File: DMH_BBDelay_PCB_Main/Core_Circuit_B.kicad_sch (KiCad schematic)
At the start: 73 parts, among them Q8 J113, SW1 SW_DPDT_3way_x2, SW2 SW_DPDT_x2, SW4 SW_SPDT, U18 CD4053B, U5 TL074, U6 TL074, U7 V3205, U8 CD4046, U9 40106

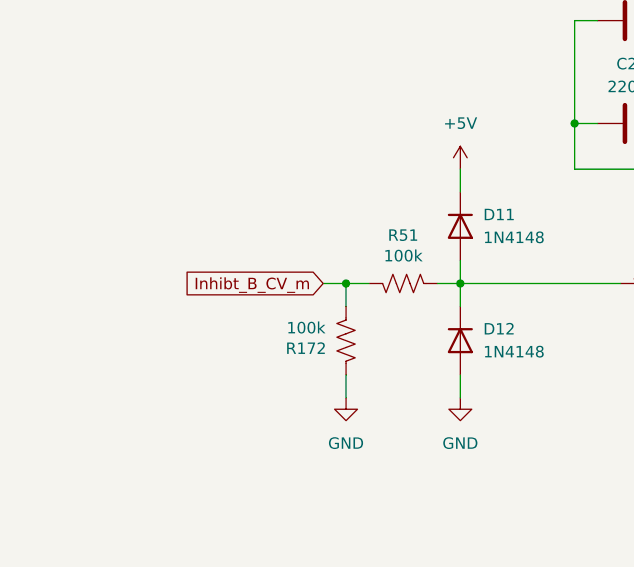
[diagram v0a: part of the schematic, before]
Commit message: Added J200 connections in IO page
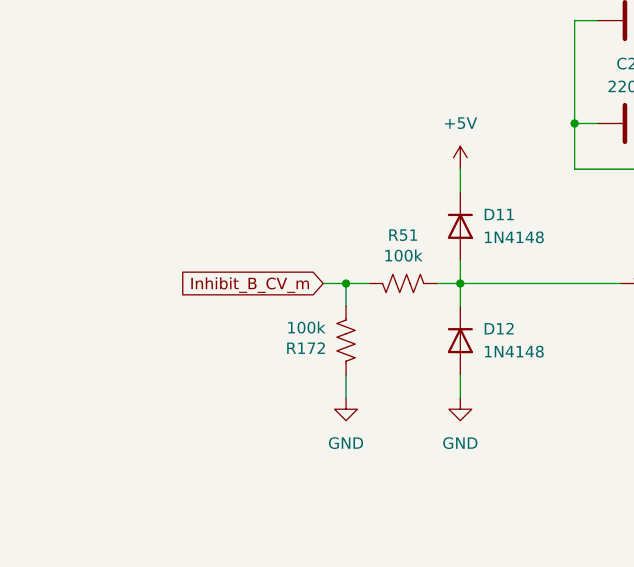
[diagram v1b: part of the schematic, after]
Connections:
- net Inhibt_B_CV_m renamed Inhibit_B_CV_m
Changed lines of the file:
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@@
 		)
 	)
-	(global_label "Inhibt_B_CV_m"
+	(global_label "Inhibit_B_CV_m"
 		(shape input)
 		(at 48.26 171.45 180)
@@
 		)
 		(property "Intersheetrefs" "${INTERSHEET_REFS}"
-			(at 31.8492 171.45 0)
+			(at 31.063 171.45 0)
 			(hide yes)
 			(show_name no)

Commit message: Highlighted Controls PCB regions
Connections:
- net Dry_B_Buff_m: no longer SW1.3 (C)
- net Dry_A_Buff_m renamed Dry_A_Buff_c
- new net Dry_B_Buff_c: SW1.3 (C)
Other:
- moved on the sheet: C35, D16, D17, D18, R105, R107, R108, R109, R110, R157, R158, R159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

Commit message: Schematic ready for breadboarding
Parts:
- added J30, J32: Conn_01x08, Connector_PinHeader_2.54mm:PinHeader_1x08_P2.54mm_Vertical, symbol Connector_Generic:Conn_01x08
- added J31, J33: Conn_01x08, Connector_PinSocket_2.54mm:PinSocket_1x08_P2.54mm_Vertical, symbol Connector_Generic:Conn_01x08
- SW1, SW2: footprint (none) -> SynthStuff:Toggle_Switch_2_Poles_TE
- SW4: footprint (none) -> SynthStuff:Toggle_Switch_TE
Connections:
- net B_Dry_Buff_Sw_m is gone; now on net Dry_B_Buff_Sw_m: U18.4 (C)
- net B_Dry_Buff_m is gone; now on net Dry_B_Buff_m: U18.3 (C1)
- net Clock_B_c: now also J31.4 (Pin_4)
- net Clock_B_m: now also J30.4 (Pin_4)
- net Clock_Cap1_B_c: now also J31.5 (Pin_5)
- net Clock_Cap1_B_m: now also J30.5 (Pin_5)
- net Clock_Cap2_B_c: now also J31.6 (Pin_6)
- net Clock_Cap2_B_m: now also J30.6 (Pin_6)
- net DW_B_CV_In_c: now also J33.7 (Pin_7)
- net DW_B_CV_In_m: now also J32.7 (Pin_7)
- net DW_B_CV_Pot_c: now also J33.6 (Pin_6)
- net DW_B_CV_Pot_m: now also J32.6 (Pin_6)
- net DW_B_Pot_c: now also J33.8 (Pin_8)
- net DW_B_Pot_m: now also J32.8 (Pin_8)
- net Dry_B_Buff_c: now also J31.3 (Pin_3)
- net Dry_B_Buff_m: now also J30.3 (Pin_3)
- net FB_B_CV_Proc_c: now also J33.2 (Pin_2)
- net FB_B_CV_Proc_m: now also J32.2 (Pin_2)
- net GND: now also J30.1 (Pin_1), J31.1 (Pin_1), J32.1 (Pin_1), J33.1 (Pin_1)
- net Link_Sw_c: now also J31.2 (Pin_2)
- net Link_Sw_m: now also J30.2 (Pin_2)
- net Time_B_CV_Proc_c: now also J33.4 (Pin_4)
- net Time_B_CV_Proc_m: now also J32.4 (Pin_4)
- net Wet_B_Out_c: now also J31.7 (Pin_7)
- net Wet_B_Out_m: now also J30.7 (Pin_7)
- net Wet_B_TC_Out_c: now also J31.8 (Pin_8)
- net Wet_B_TC_Out_m: now also J30.8 (Pin_8)
- net PP_Sw_c renamed PP_Sw_p5_c
- net PP_Sw_m renamed PP_Sw_p5_m
- net VCXF_DW_B/In_A renamed PP_Sw_p2_c
- new net FB_B_CV_In_c: J33.3 (Pin_3)
- new net FB_B_CV_In_m: J32.3 (Pin_3)
- new net Time_B_CV_In_c: J33.5 (Pin_5)
- new net Time_B_CV_In_m: J32.5 (Pin_5)
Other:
- moved on the sheet: SW1A, U9F, U9G

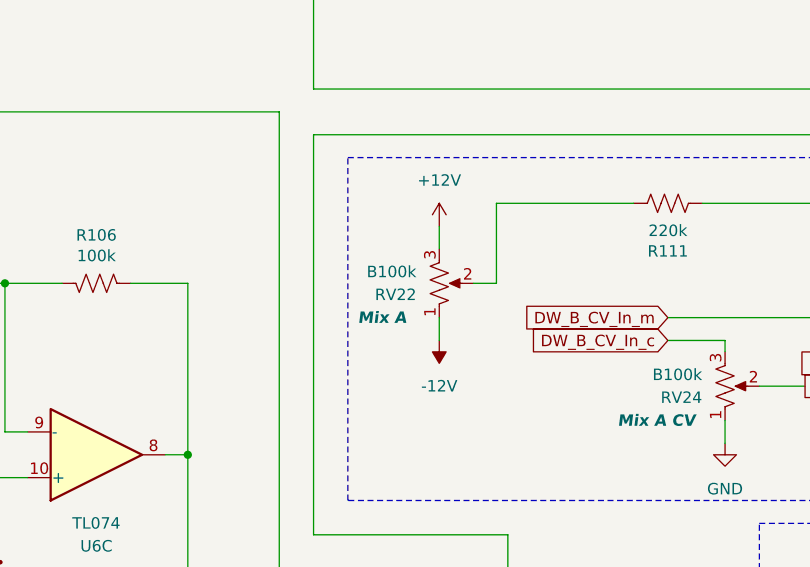
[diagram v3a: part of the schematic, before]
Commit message: Reversed mix pots polarity
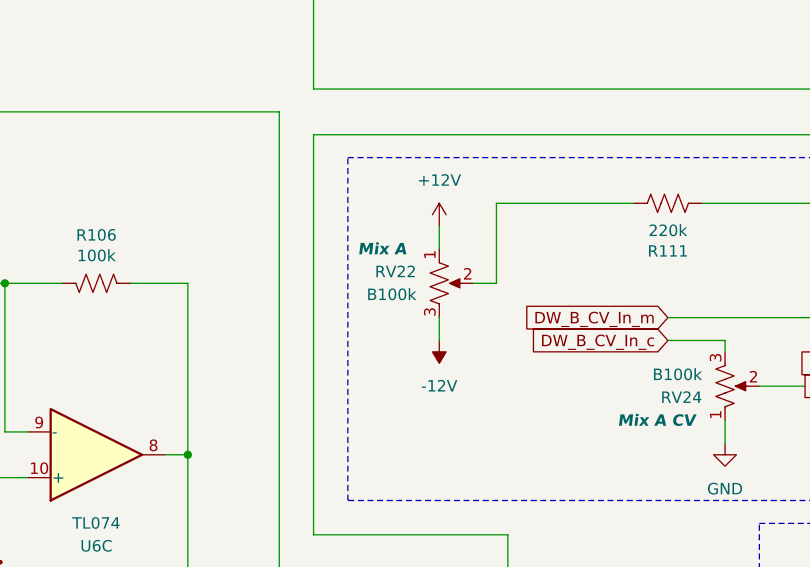
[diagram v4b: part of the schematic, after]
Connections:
- net +12V: now also RV22.1; no longer RV22.3
- net -12V: now also RV22.3; no longer RV22.1
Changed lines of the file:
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@@
 		(lib_id "Device:R_Potentiometer_US")
 		(at 292.1 50.8 0)
-		(mirror x)
 		(unit 1)
 		(body_style 1)
@@
 		(dnp no)
 		(property "Reference" "RV22"
-			(at 289.56 52.0701 0)
+			(at 289.56 49.5299 0)
 			(show_name no)
 			(do_not_autoplace no)
@@
 		)
 		(property "Value" "B100k"
-			(at 289.56 49.5301 0)
+			(at 289.56 52.0699 0)
 			(show_name no)
 			(do_not_autoplace no)
@@
 		)
 		(property "Function" "Mix A"
-			(at 285.75 54.61 0)
+			(at 285.75 46.99 0)
 			(show_name no)
 			(do_not_autoplace no)

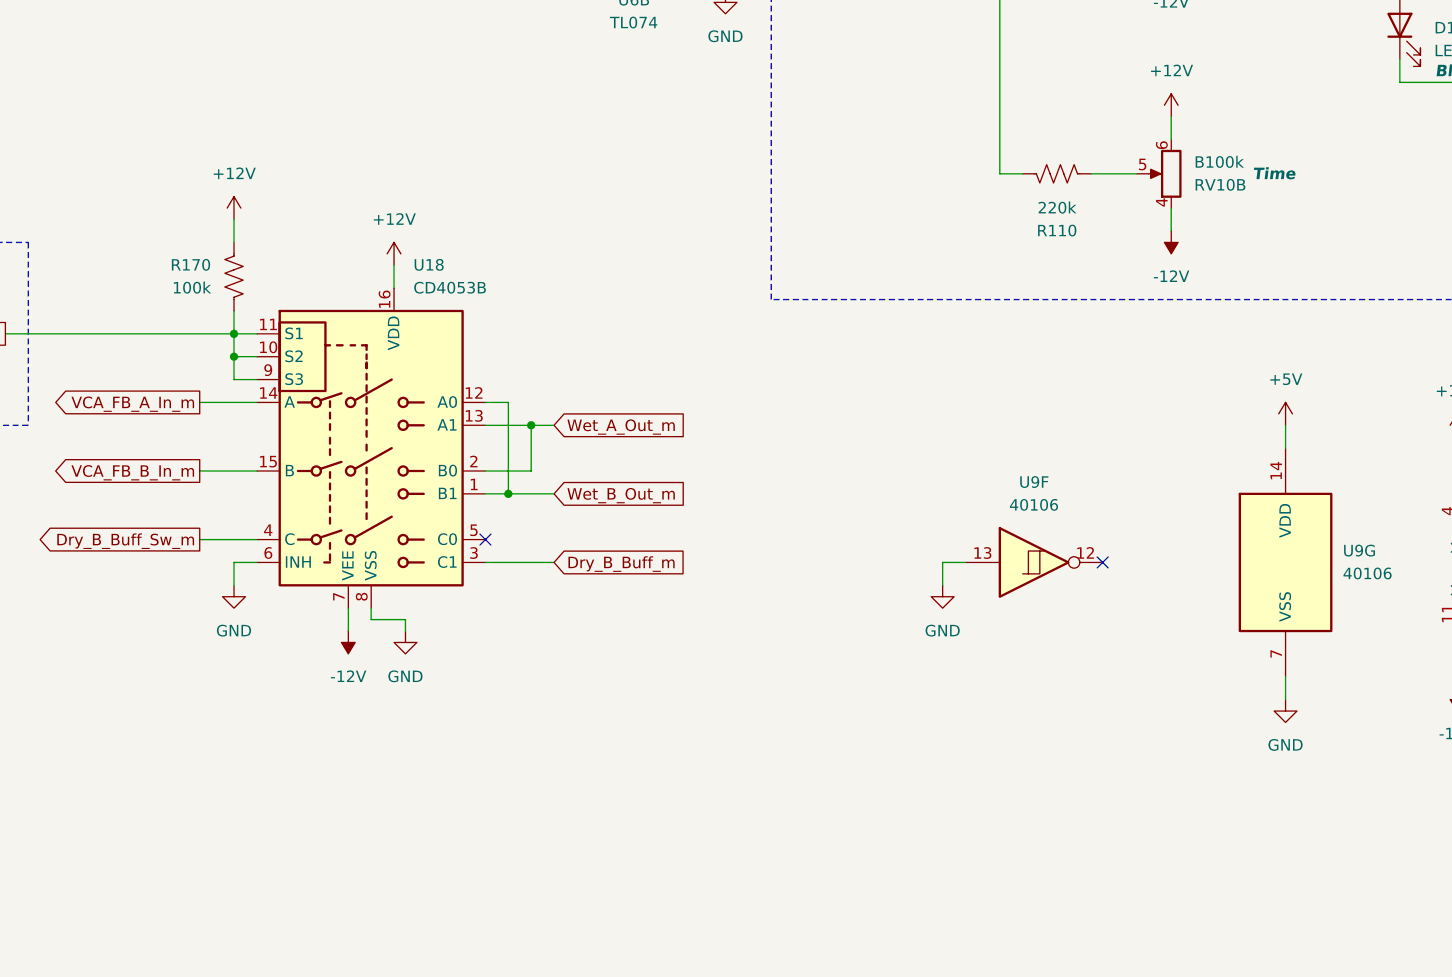
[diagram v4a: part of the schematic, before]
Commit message: Added CMOS ICs decoupling caps
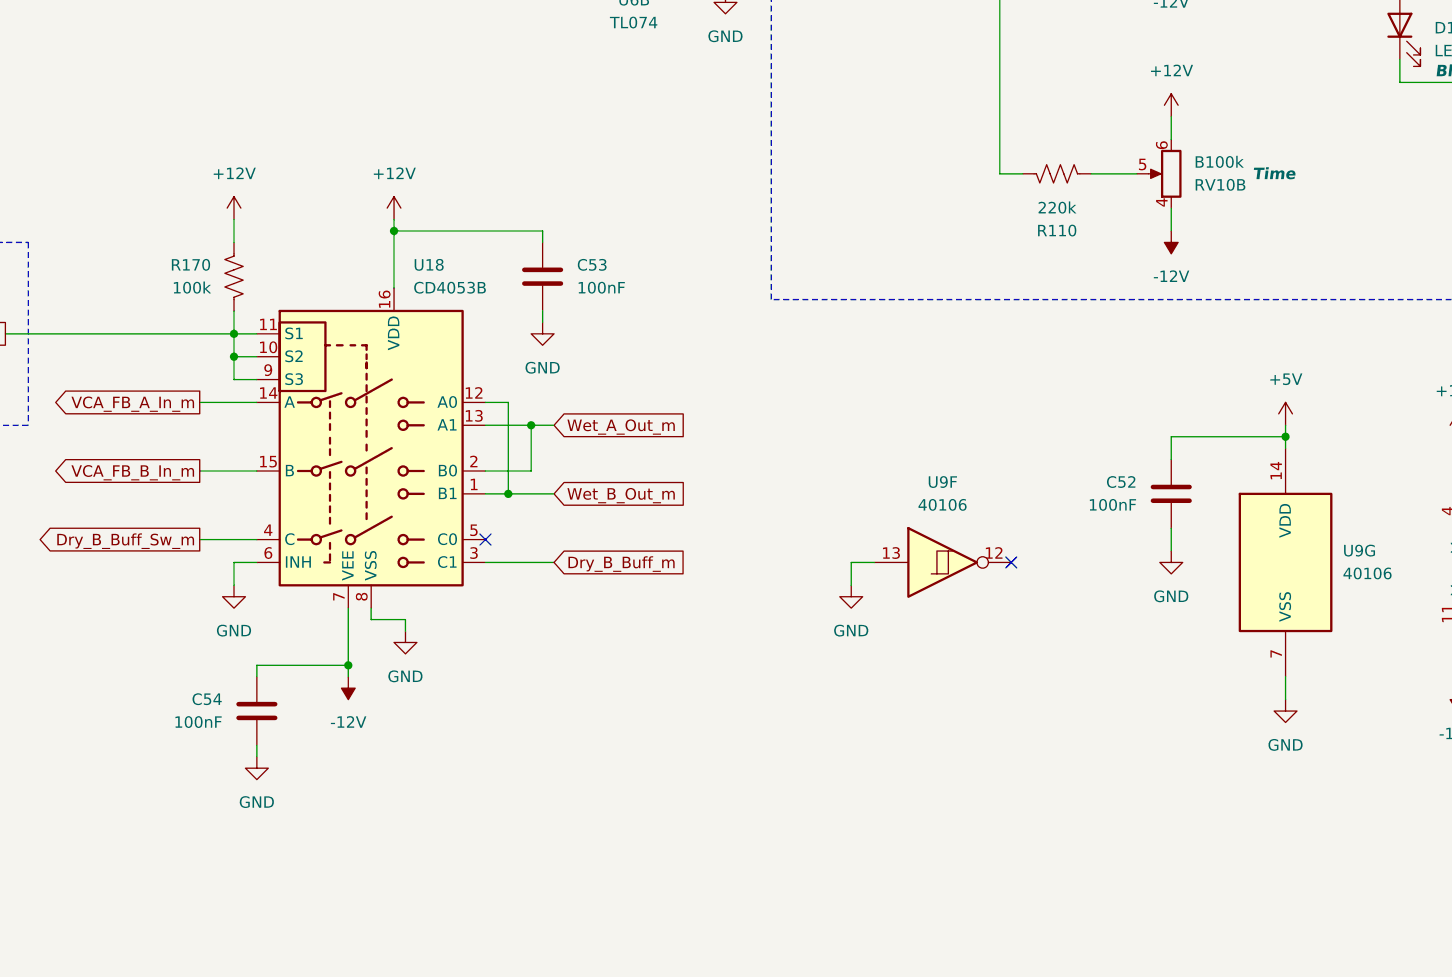
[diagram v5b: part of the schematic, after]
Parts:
- added C52, C53, C54: 100nF, Capacitor_THT:C_Disc_D4.3mm_W1.9mm_P5.00mm, symbol Device:C
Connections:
- net +12V: now also C53.1
- net +5V: now also C52.1
- net -12V: now also C54.1
- net GND: now also C52.2, C53.2, C54.2
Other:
- moved on the sheet: U9F

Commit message: Moved LEDs to own page
... so I can add the LED control via CD4040
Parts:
- removed D16: LED_Blue, LED_THT:LED_D3.0mm, symbol Device:LED
- removed D17, D18: LED_Red, LED_THT:LED_D3.0mm, symbol Device:LED
- removed R157: 4k7, Resistor_THT:R_Axial_DIN0207_L6.3mm_D2.5mm_P7.62mm_Horizontal, symbol Device:R_US
- removed R158, R159: 3k3, Resistor_THT:R_Axial_DIN0207_L6.3mm_D2.5mm_P7.62mm_Horizontal, symbol Device:R_US
- removed unit 2 of SW2
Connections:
- net +5V: no longer U8.14 (SigIn)
- net Clock_B_m: no longer U8.3 (RefIn)
- no-connect marks 11 -> 13

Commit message: Added clock dividers for LEDs
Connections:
- net GND: no longer J32.1 (Pin_1), J33.1 (Pin_1)
- net Clock_B_Inv_m: now reaches U7.2 (CP2), U9.2
- net Clock_B_Inv_m: now also J32.1 (Pin_1)
- new net Clock_B_Inv_c: J33.1 (Pin_1)
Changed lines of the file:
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@@
 	)
 	(junction
+		(at 180.34 91.44)
+		(diameter 0)
+		(color 0 0 0 0)
+	)
+	(junction
 		(at 27.94 66.04)
 		(diameter 0)
@@
 	(wire
 		(pts
-			(xy 57.15 243.84) (xy 41.91 243.84)
-		)
-		(stroke
-			(width 0)
-			(type default)
-		)
-	)
-	(wire
-		(pts
 			(xy 165.1 152.4) (xy 184.15 152.4)
 		)
@@
 	(wire
 		(pts
+			(xy 88.9 251.46) (xy 96.52 251.46)
+		)
+		(stroke
+			(width 0)
+			(type default)
+		)
+	)
+	(wire
+		(pts
+			(xy 180.34 91.44) (xy 195.58 91.44)
+		)
+		(stroke
+			(width 0)
+			(type default)
+		)
+	)
+	(wire
+		(pts
 			(xy 86.36 142.24) (xy 91.44 142.24)
 		)
@@
 	(wire
 		(pts
-			(xy 107.95 246.38) (xy 107.95 243.84)
-		)
-		(stroke
-			(width 0)
-			(type default)
-		)
-	)
-	(wire
-		(pts
 			(xy 124.46 91.44) (xy 121.92 91.44)
 		)
@@
 	(wire
 		(pts
-			(xy 92.71 251.46) (xy 96.52 251.46)
-		)
-		(stroke
-			(width 0)
-			(type default)
-		)
-	)
-	(wire
-		(pts
 			(xy 148.59 101.6) (xy 148.59 109.22)
 		)
@@
 	(wire
 		(pts
-			(xy 41.91 243.84) (xy 41.91 251.46)
-		)
-		(stroke
-			(width 0)
-			(type default)
-		)
-	)
-	(wire
-		(pts
 			(xy 267.97 149.86) (xy 267.97 157.48)
 		)
@@
 	(wire
 		(pts
-			(xy 41.91 251.46) (xy 45.72 251.46)
-		)
-		(stroke
-			(width 0)
-			(type default)
-		)
-	)
-	(wire
-		(pts
 			(xy 124.46 91.44) (xy 143.51 91.44)
 		)
@@
 	(wire
 		(pts
-			(xy 92.71 243.84) (xy 92.71 251.46)
-		)
-		(stroke
-			(width 0)
-			(type default)
-		)
-	)
-	(wire
-		(pts
 			(xy 88.9 256.54) (xy 96.52 256.54)
 		)
@@
 	(wire
 		(pts
-			(xy 38.1 222.25) (xy 45.72 222.25)
+			(xy 38.1 251.46) (xy 45.72 251.46)
 		)
 		(stroke
@@
 	(wire
 		(pts
-			(xy 317.5 57.15) (xy 323.85 57.15)
+			(xy 38.1 222.25) (xy 45.72 222.25)
 		)
 		(stroke
@@
 	(wire
 		(pts
-			(xy 264.16 97.79) (xy 264.16 99.06)
+			(xy 317.5 57.15) (xy 323.85 57.15)
 		)
 		(stroke
@@
 	(wire
 		(pts
-			(xy 107.95 243.84) (xy 92.71 243.84)
+			(xy 264.16 97.79) (xy 264.16 99.06)
 		)
 		(stroke
@@
 	(wire
 		(pts
-			(xy 57.15 246.38) (xy 57.15 243.84)
-		)
-		(stroke
-			(width 0)
-			(type default)
-		)
-	)
-	(wire
-		(pts
 			(xy 264.16 97.79) (xy 278.13 97.79)
 		)
@@
 		)
 	)
+	(global_label "Clock_B_Inv_m"
+		(shape passive)
+		(at 38.1 251.46 180)
+		(fields_autoplaced yes)
+		(effects
+			(font
+				(size 1.27 1.27)
+			)
+			(justify right)
+		)
+		(property "Intersheetrefs" "${INTERSHEET_REFS}"
+			(at 22.4377 251.46 0)
+			(hide yes)
+			(show_name no)
+			(do_not_autoplace no)
+			(effects
+				(font
+					(size 1.27 1.27)
+				)
+				(justify right)
+			)
+		)
+	)
 	(global_label "Wet_B_TC_Out_m"
 		(shape input)
@@
 		)
 	)
+	(global_label "Clock_B_Inv_c"
+		(shape passive)
+		(at 88.9 251.46 180)
+		(fields_autoplaced yes)
+		(effects
+			(font
+				(size 1.27 1.27)
+			)
+			(justify right)
+		)
+		(property "Intersheetrefs" "${INTERSHEET_REFS}"
+			(at 73.8424 251.46 0)
+			(hide yes)
+			(show_name no)
+			(do_not_autoplace no)
+			(effects
+				(font
+					(size 1.27 1.27)
+				)
+				(justify right)
+			)
+		)
+	)
 	(global_label "FB_B_CV_Proc_m"
 		(shape passive)
@@
 		)
 	)
+	(global_label "Clock_B_Inv_m"
+		(shape output)
+		(at 195.58 91.44 0)
+		(fields_autoplaced yes)
+		(effects
+			(font
+				(size 1.27 1.27)
+			)
+			(justify left)
+		)
+		(property "Intersheetrefs" "${INTERSHEET_REFS}"
+			(at 212.3536 91.44 0)
+			(hide yes)
+			(show_name no)
+			(do_not_autoplace no)
+			(effects
+				(font
+					(size 1.27 1.27)
+				)
+				(justify left)
+			)
+		)
+	)
 	(global_label "DW_B_Pot_m"
 		(shape input)
@@
 	)
 	(symbol
-		(lib_id "power:GND")
-		(at 107.95 246.38 0)
-		(unit 1)
-		(body_style 1)
-		(exclude_from_sim no)
-		(in_bom yes)
-		(on_board yes)
-		(in_pos_files yes)
-		(dnp no)
-		(fields_autoplaced yes)
-		(property "Reference" "#PWR0212"
-			(at 107.95 252.73 0)
-			(hide yes)
-			(show_name no)
-			(do_not_autoplace no)
-			(effects
-				(font
-					(size 1.27 1.27)
-				)
-			)
-		)
-		(property "Value" "GND"
-			(at 107.95 251.46 0)
-			(show_name no)
-			(do_not_autoplace no)
-			(effects
-				(font
-					(size 1.27 1.27)
-				)
-			)
-		)
-		(property "Footprint" ""
-			(at 107.95 246.38 0)
-			(hide yes)
-			(show_name no)
-			(do_not_autoplace no)
-			(effects
-				(font
-					(size 1.27 1.27)
-				)
-			)
-		)
-		(property "Datasheet" ""
-			(at 107.95 246.38 0)
-			(hide yes)
-			(show_name no)
-			(do_not_autoplace no)
-			(effects
-				(font
-					(size 1.27 1.27)
-				)
-			)
-		)
-		(property "Description" "Power symbol creates a global label with name \"GND\" , ground"
-			(at 107.95 246.38 0)
-			(hide yes)
-			(show_name no)
-			(do_not_autoplace no)
-			(effects
-				(font
-					(size 1.27 1.27)
-				)
-			)
-		)
-		(pin "1"
-		)
-		(instances
-			(project "DMH_BBDelay_PCB_Main"
-				(path "/58f4306d-5387-4983-bb08-41a2313fd315/53120047-129a-4e0f-876f-6cafa2f18733"
-					(reference "#PWR0212")
-					(unit 1)
-				)
-			)
-		)
-	)
-	(symbol
 		(lib_id "power:+5V")
 		(at 184.15 139.7 0)
@@
 					(unit 1)
 				)
-			)
-		)
-	)
-	(symbol
-		(lib_id "power:GND")
-		(at 57.15 246.38 0)
-		(unit 1)
-		(body_style 1)
-		(exclude_from_sim no)
-		(in_bom yes)
-		(on_board yes)
-		(in_pos_files yes)
-		(dnp no)
-		(fields_autoplaced yes)
-		(property "Reference" "#PWR018"
-			(at 57.15 252.73 0)
-			(hide yes)
-			(show_name no)
-			(do_not_autoplace no)
-			(effects
-				(font
-					(size 1.27 1.27)
-				)
-			)
-		)
-		(property "Value" "GND"
-			(at 57.15 251.46 0)
-			(show_name no)
-			(do_not_autoplace no)
-			(effects
-				(font
-					(size 1.27 1.27)
-				)
-			)
-		)
-		(property "Footprint" ""
-			(at 57.15 246.38 0)
-			(hide yes)
-			(show_name no)
-			(do_not_autoplace no)
-			(effects
-				(font
-					(size 1.27 1.27)
-				)
-			)
-		)
-		(property "Datasheet" ""
-			(at 57.15 246.38 0)
-			(hide yes)
-			(show_name no)
-			(do_not_autoplace no)
-			(effects
-				(font
-					(size 1.27 1.27)
-				)
-			)
-		)
-		(property "Description" "Power symbol creates a global label with name \"GND\" , ground"
-			(at 57.15 246.38 0)
-			(hide yes)
-			(show_name no)
-			(do_not_autoplace no)
-			(effects
-				(font
-					(size 1.27 1.27)
-				)
-			)
-		)
-		(pin "1"
-		)
-		(instances
-			(project "DMH_BBDelay_PCB_Main"
-				(path "/58f4306d-5387-4983-bb08-41a2313fd315/53120047-129a-4e0f-876f-6cafa2f18733"
-					(reference "#PWR018")
-					(unit 1)
-				)
